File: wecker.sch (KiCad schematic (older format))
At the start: 2 parts, among them J1 Conn_01x20, U1 MSP430FR4133

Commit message: added some more parts
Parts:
- added C1, C2, C3, C4: 0.1µF, Capacitor_SMD:C_1206_3216Metric_Pad1.42x1.75mm_HandSolder, symbol Device:C
- added D1, D2: LED_BG, LED_SMD:LED_1210_3225Metric_Pad1.42x2.65mm_HandSolder, symbol Device:LED
- added J2: Conn_01x05_Male, Connector_PinHeader_2.54mm:PinHeader_1x05_P2.54mm_Horizontal, symbol Connector:Conn_01x05_Male
- added Q1: PN2222A, Package_TO_SOT_THT:TO-92_Inline, symbol Transistor_BJT:PN2222A
- added R1: R, Resistor_SMD:R_1210_3225Metric_Pad1.42x2.65mm_HandSolder, symbol Device:R
- added SW1: Hour, Button_Switch_SMD:SW_SPST_B3U-1000P, symbol Switch:SW_Push
- added SW2: Minute, Button_Switch_SMD:SW_SPST_B3U-1000P, symbol Switch:SW_Push
- added SW3: Snooze, Button_Switch_SMD:SW_SPST_B3U-1000P, symbol Switch:SW_Push
- added TP1: ClockInput, Connector_Wire:SolderWirePad_1x01_Drill1.2mm, symbol Connector:TestPoint
- added Y1: 32.768 kHz, Crystal:Crystal_HC18-U_Horizontal, symbol Device:Crystal_Small
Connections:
- net labels added: +BATT, GND
- wire segments 80 -> 162

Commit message: exchange some parts
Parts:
- removed Q1: PN2222A, Package_TO_SOT_THT:TO-92_Inline, symbol Transistor_BJT:PN2222A
- added Q1: BC818, Package_TO_SOT_SMD:SOT-23, symbol Transistor_BJT:BC818
- J2: footprint Connector_PinHeader_2.54mm:PinHeader_1x05_P2.54mm_Horizontal -> Connector_PinHeader_2.54mm:PinHeader_1x05_P2.54mm_Vertical
- Y1: footprint Crystal:Crystal_HC18-U_Horizontal -> Crystal:Crystal_DS26_D2.0mm_L6.0mm_Horizontal
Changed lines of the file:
@@
 F 0 "Y1" H 2600 4850 50  0000 C CNN
 F 1 "32.768 kHz" H 2600 5050 50  0000 C CNN
-F 2 "Crystal:Crystal_HC18-U_Horizontal" H 2600 4950 50  0001 C CNN
+F 2 "Crystal:Crystal_DS26_D2.0mm_L6.0mm_Horizontal" H 2600 4950 50  0001 C CNN
 F 3 "~" H 2600 4950 50  0001 C CNN
 	1    2600 4950
@@
 F 0 "J2" V 5112 3194 50  0000 L CNN
 F 1 "Conn_01x05_Male" V 5203 3194 50  0000 L CNN
-F 2 "Connector_PinHeader_2.54mm:PinHeader_1x05_P2.54mm_Horizontal" H 5050 2950 50  0001 C CNN
+F 2 "Connector_PinHeader_2.54mm:PinHeader_1x05_P2.54mm_Vertical" H 5050 2950 50  0001 C CNN
 F 3 "~" H 5050 2950 50  0001 C CNN
 	1    5050 2950
@@
 	9050 4550 9450 4550
 $Comp
-L Transistor_BJT:PN2222A Q1
-U 1 1 5DB2D7A4
-P 9650 4550
-F 0 "Q1" H 9840 4596 50  0000 L CNN
-F 1 "PN2222A" H 9840 4505 50  0000 L CNN
-F 2 "Package_TO_SOT_THT:TO-92_Inline" H 9850 4475 50  0001 L CIN
-F 3 "http://www.fairchildsemi.com/ds/PN/PN2222A.pdf" H 9650 4550 50  0001 L CNN
-	1    9650 4550
-	1    0    0    -1
-$EndComp
-$Comp
 L power:+BATT #PWR0108
 U 1 1 5DB2F2CF
@@
 Wire Wire Line
 	9750 4850 9750 4750
+$Comp
+L Transistor_BJT:BC818 Q1
+U 1 1 5DA08DFD
+P 9650 4550
+F 0 "Q1" H 9841 4596 50  0000 L CNN
+F 1 "BC818" H 9841 4505 50  0000 L CNN
+F 2 "Package_TO_SOT_SMD:SOT-23" H 9850 4475 50  0001 L CIN
+F 3 "https://www.fairchildsemi.com/datasheets/BC/BC818.pdf" H 9650 4550 50  0001 L CNN
+	1    9650 4550
+	1    0    0    -1
+$EndComp
 $EndSCHEMATC

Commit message: correct PCB Measurements
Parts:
- J2: symbol Connector:Conn_01x05_Male -> wecker-rescue:Conn_01x05_Male-Connector
- TP1: symbol Connector:TestPoint -> wecker-rescue:TestPoint-Connector
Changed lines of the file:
@@
 $EndComp
 $Comp
-L Connector:TestPoint TP1
+L wecker-rescue:TestPoint-Connector TP1
 U 1 1 5DAABA72
 P 7250 4550
@@
 	7900 5050 5350 5050
 $Comp
-L Connector:Conn_01x05_Male J2
+L wecker-rescue:Conn_01x05_Male-Connector J2
 U 1 1 5DAD772A
 P 5050 2950

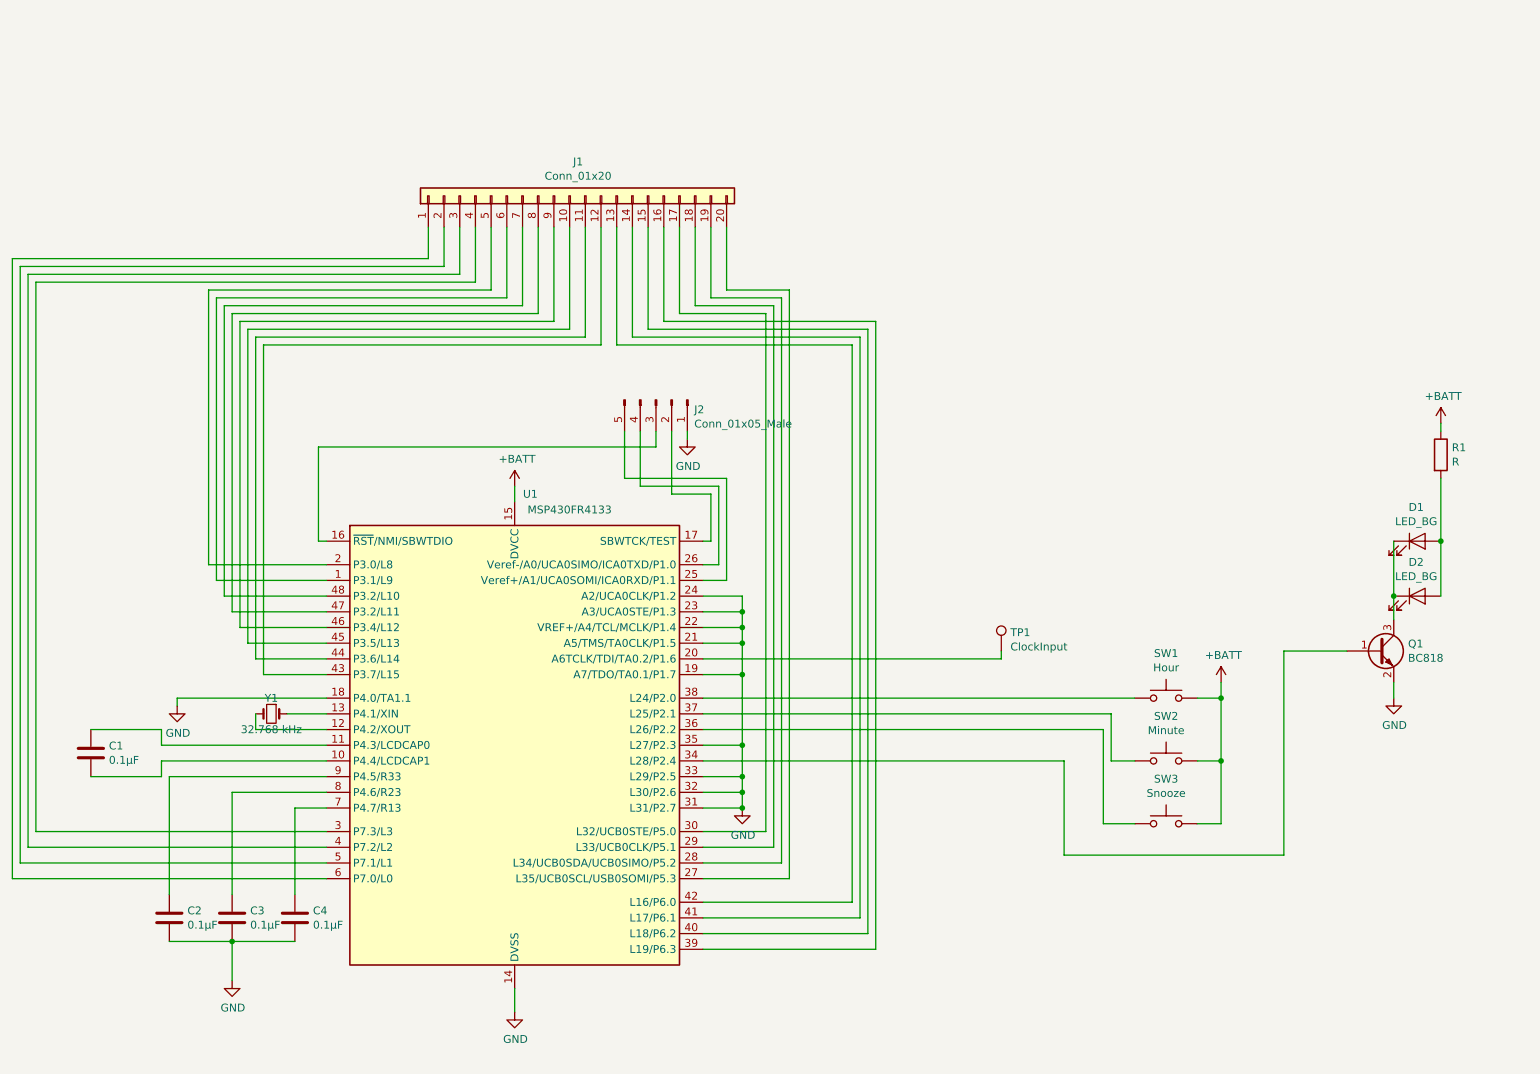
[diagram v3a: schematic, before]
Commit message: added Buzzer make LCD Bus
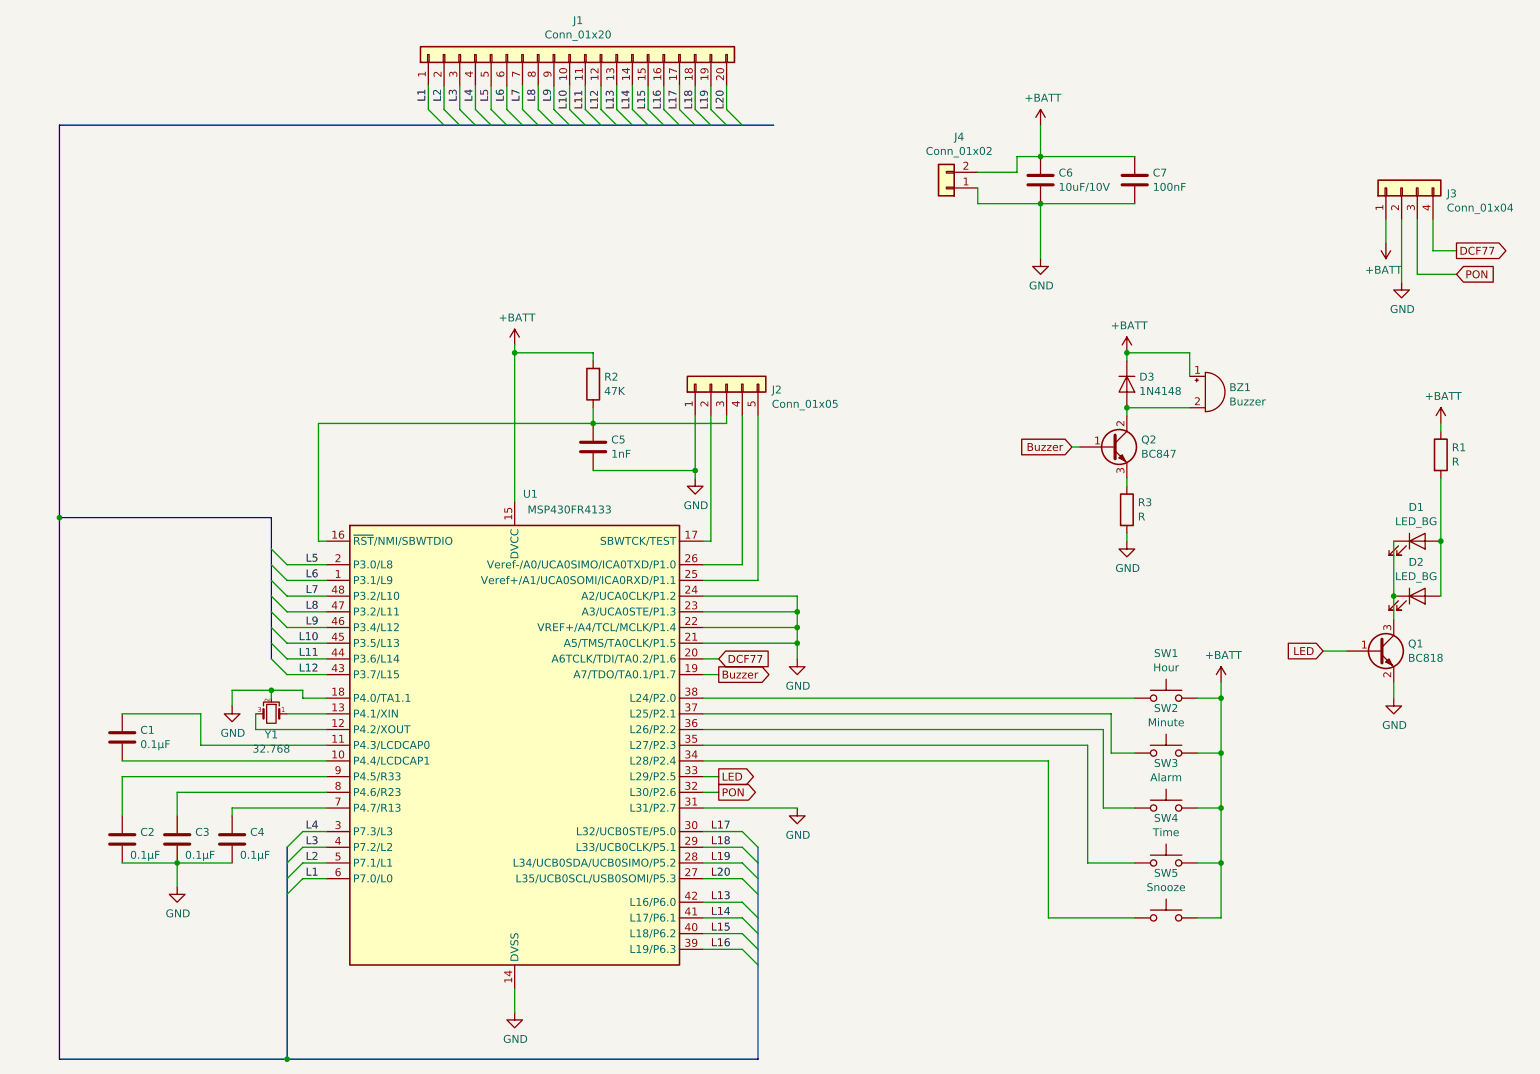
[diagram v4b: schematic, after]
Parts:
- removed J2: Conn_01x05_Male, Connector_PinHeader_2.54mm:PinHeader_1x05_P2.54mm_Vertical, symbol wecker-rescue:Conn_01x05_Male-Connector
- removed TP1: ClockInput, Connector_Wire:SolderWirePad_1x01_Drill1.2mm, symbol wecker-rescue:TestPoint-Connector
- removed Y1: 32.768 kHz, Crystal:Crystal_DS26_D2.0mm_L6.0mm_Horizontal, symbol Device:Crystal_Small
- added BZ1: Buzzer, symbol Device:Buzzer
- added C5: 1nF, symbol Device:C
- added C6: 10uF/10V, symbol Device:C
- added C7: 100nF, symbol Device:C
- added D3: 1N4148, symbol Device:D
- added J2: Conn_01x05, symbol Connector_Generic:Conn_01x05
- added J3: Conn_01x04, symbol Connector_Generic:Conn_01x04
- added J4: Conn_01x02, symbol Connector_Generic:Conn_01x02
- added Q2: BC847, symbol Device:Q_NPN_BCE
- added R2: 47K, symbol Device:R
- added R3: R, symbol Device:R
- added SW4: Time, Button_Switch_SMD:SW_SPST_B3U-1000P, symbol Switch:SW_Push
- added SW5: Snooze, Button_Switch_SMD:SW_SPST_B3U-1000P, symbol Switch:SW_Push
- added Y1: 32.768, symbol Device:Crystal_GND2_Small
- SW3: value Snooze -> Alarm
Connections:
- net +BATT: now also BZ1.1 (-), C6.1, C7.1, D3.1 (K), J3.1 (Pin_1), J4.2 (Pin_2), R2.2, SW4.2, SW5.2
- net GND: now also C5.1, C6.2, C7.2, J2.1 (Pin_1), J3.2 (Pin_2), J4.1 (Pin_1), R3.2, Y1.2; no longer U1.19 (A7/TDO/TA0.1/P1.7), U1.32 (L30/P2.6), U1.33 (L29/P2.5), U1.35 (L27/P2.3)
- net L6: now reaches J1.6 (Pin_6), U1.1 (P3.1/L9)
- net at U1.12 (P4.2/XOUT): now also Y1.3
- net at U1.13 (P4.1/XIN): now also Y1.1
- net at U1.16 (~RST~/NMI/SBWTDIO): now also C5.2, J2.3 (Pin_3), R2.1
- net at U1.17 (SBWTCK/TEST): now also J2.2 (Pin_2)
- net L5: now reaches J1.5 (Pin_5), U1.2 (P3.0/L8)
- net DCF77: now reaches U1.20 (A6TCLK/TDI/TA0.2/P1.6)
- net DCF77: now also J3.4 (Pin_4)
- net at U1.25 (Veref+/A1/UCA0SOMI/ICA0RXD/P1.1): now also J2.5 (Pin_5)
- net at U1.26 (Veref-/A0/UCA0SIMO/ICA0TXD/P1.0): now also J2.4 (Pin_4)
- net L20: now reaches J1.20 (Pin_20), U1.27 (L35/UCB0SCL/USB0SOMI/P5.3)
- net L19: now reaches J1.19 (Pin_19), U1.28 (L34/UCB0SDA/UCB0SIMO/P5.2)
- net L18: now reaches J1.18 (Pin_18), U1.29 (L33/UCB0CLK/P5.1)
- net L4: now reaches J1.4 (Pin_4), U1.3 (P7.3/L3)
- net L17: now reaches J1.17 (Pin_17), U1.30 (L32/UCB0STE/P5.0)
- net at U1.34 (L28/P2.4): now also SW5.1; no longer Q1.1 (B)
- net L16: now reaches J1.16 (Pin_16), U1.39 (L19/P6.3)
- net L3: now reaches J1.3 (Pin_3), U1.4 (P7.2/L2)
- net L15: now reaches J1.15 (Pin_15), U1.40 (L18/P6.2)
- net L14: now reaches J1.14 (Pin_14), U1.41 (L17/P6.1)
- net L13: now reaches J1.13 (Pin_13), U1.42 (L16/P6.0)
- net L12: now reaches J1.12 (Pin_12), U1.43 (P3.7/L15)
- net L11: now reaches J1.11 (Pin_11), U1.44 (P3.6/L14)
- net L10: now reaches J1.10 (Pin_10), U1.45 (P3.5/L13)
- net L9: now reaches J1.9 (Pin_9), U1.46 (P3.4/L12)
- net L8: now reaches J1.8 (Pin_8), U1.47 (P3.2/L11)
- net L7: now reaches J1.7 (Pin_7), U1.48 (P3.2/L10)
- net L2: now reaches J1.2 (Pin_2), U1.5 (P7.1/L1)
- net L1: now reaches J1.1 (Pin_1), U1.6 (P7.0/L0)
- new net: SW4.1, U1.35 (L27/P2.3)
- new net: BZ1.2 (+), D3.2 (A), Q2.2 (C)
- new net: Q2.3 (E), R3.1
- new net Buzzer: Q2.1 (B), U1.19 (A7/TDO/TA0.1/P1.7)
- new net LED: Q1.1 (B), U1.33 (L29/P2.5)
- new net PON: J3.3 (Pin_3), U1.32 (L30/P2.6)
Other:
- moved on the sheet: C1, C2, C3, C4, J1, SW2, SW3

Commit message: still not ready
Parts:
- added C8, C9: 12p, Capacitor_SMD:C_0603_1608Metric_Pad1.05x0.95mm_HandSolder, symbol Device:C_Small
- BZ1: footprint (none) -> Buzzer_Beeper:Buzzer_12x9.5RM7.6
- C1: value 0.1µF -> 1u; symbol Device:C -> Device:C_Small
- C2, C3, C4: value 0.1µF -> 100n; symbol Device:C -> Device:C_Small
- C5: footprint (none) -> Capacitor_SMD:C_1206_3216Metric_Pad1.42x1.75mm_HandSolder
- C6: value 10uF/10V -> 10u/10V; footprint (none) -> Capacitor_SMD:C_0603_1608Metric_Pad1.05x0.95mm_HandSolder
- C7: value 100nF -> 100n; footprint (none) -> Capacitor_SMD:C_1206_3216Metric_Pad1.42x1.75mm_HandSolder
- D3: footprint (none) -> Diode_SMD:D_0805_2012Metric_Pad1.15x1.40mm_HandSolder
- J2: footprint (none) -> Connector_PinHeader_2.54mm:PinHeader_1x05_P2.54mm_Horizontal
- J3: footprint (none) -> Connector_PinHeader_2.54mm:PinHeader_1x04_P2.54mm_Horizontal
- J4: footprint (none) -> Connector_PinHeader_2.54mm:PinHeader_1x02_P2.54mm_Horizontal
- Q2: value BC847 -> BC847; footprint (none) -> Package_TO_SOT_SMD:SOT-23
- R1: footprint Resistor_SMD:R_1210_3225Metric_Pad1.42x2.65mm_HandSolder -> Resistor_SMD:R_0603_1608Metric_Pad1.05x0.95mm_HandSolder
- R2, R3: footprint (none) -> Resistor_SMD:R_0603_1608Metric_Pad1.05x0.95mm_HandSolder
- Y1: footprint (none) -> Crystal:Crystal_DS26_D2.0mm_L6.0mm_Horizontal_1EP_style1
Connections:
- net GND: now also C8.2, C9.2; no longer U1.18 (P4.0/TA1.1), U1.21 (A5/TMS/TA0CLK/P1.5), U1.22 (VREF+/A4/TCL/MCLK/P1.4), U1.23 (A3/UCA0STE/P1.3), U1.24 (A2/UCA0CLK/P1.2), U1.31 (L31/P2.7)
- net at U1.12 (P4.2/XOUT), Y1.3: now also C9.1
- net at U1.13 (P4.1/XIN), Y1.1: now also C8.1
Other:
- note added: "DNP"
- moved on the sheet: C1, C2, C3, C4, Y1

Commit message: some more corrections
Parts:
- removed D3: 1N4148, Diode_SMD:D_0805_2012Metric_Pad1.15x1.40mm_HandSolder, symbol Device:D
- added R4: 1k, Resistor_SMD:R_0805_2012Metric_Pad1.15x1.40mm_HandSolder, symbol Device:R
- BZ1: footprint Buzzer_Beeper:Buzzer_12x9.5RM7.6 -> Buzzer_Beeper:Buzzer_TDK_PS1240P02BT_D12.2mm_H6.5mm
- C1, C2, C3, C4, C5, C7: footprint Capacitor_SMD:C_1206_3216Metric_Pad1.42x1.75mm_HandSolder -> Capacitor_SMD:C_0805_2012Metric_Pad1.15x1.40mm_HandSolder
- C6, C8, C9: footprint Capacitor_SMD:C_0603_1608Metric_Pad1.05x0.95mm_HandSolder -> Capacitor_SMD:C_0805_2012Metric_Pad1.15x1.40mm_HandSolder
- R1, R3: value R -> 1K; footprint Resistor_SMD:R_0603_1608Metric_Pad1.05x0.95mm_HandSolder -> Resistor_SMD:R_0805_2012Metric_Pad1.15x1.40mm_HandSolder
- R2: footprint Resistor_SMD:R_0603_1608Metric_Pad1.05x0.95mm_HandSolder -> Resistor_SMD:R_0805_2012Metric_Pad1.15x1.40mm_HandSolder
- Y1: symbol Device:Crystal_GND2_Small -> Device:Crystal_GND3_Small
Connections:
- net +BATT: now also D1.2 (A), D2.2 (A), R4.1; no longer R1.1
- net Buzzer: now also R3.1; no longer Q2.1 (B)
- net GND: now also Q2.3 (E); no longer C8.2, C9.2, R3.2, Y1.2
- net LED: now also R1.1; no longer Q1.1 (B)
- net at C8.1, Y1.1: now also U1.12 (P4.2/XOUT); no longer U1.13 (P4.1/XIN)
- net at BZ1.2 (+), Q2.2 (C): now also R4.2
- new net: C9.1, U1.13 (P4.1/XIN), Y1.2
- new net: Q1.1 (B), R1.2
- new net: Q2.1 (B), R3.2
- new net GNDS: C8.2, C9.2, Y1.3
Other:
- moved on the sheet: D1, D2, Q1, R1, R3

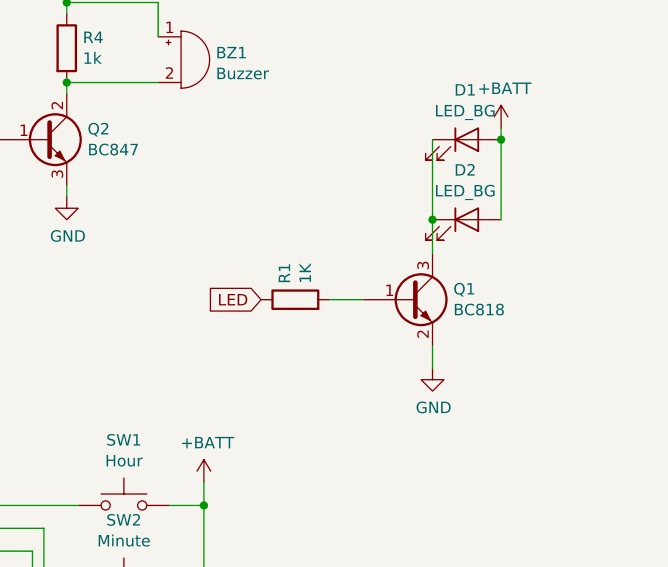
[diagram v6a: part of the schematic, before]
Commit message: set LED Rb and Tr Type
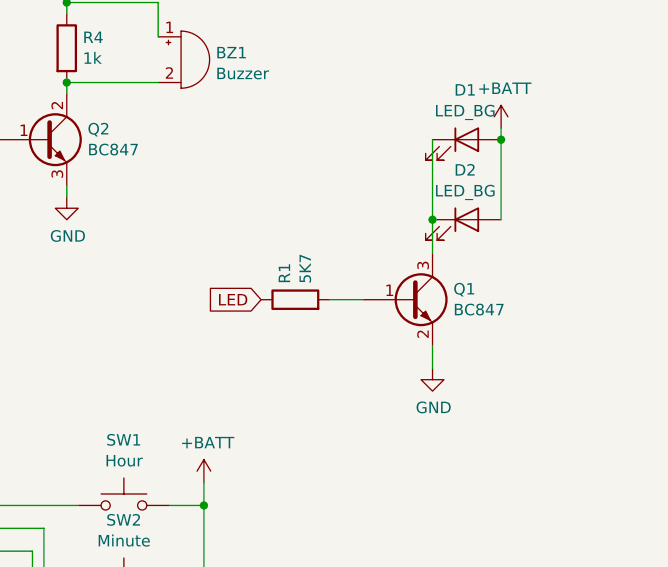
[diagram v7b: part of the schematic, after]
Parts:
- Q1: value BC818 -> BC847
- R1: value 1K -> 5K7
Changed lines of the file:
@@
 P 9050 3950
 F 0 "R1" H 9120 3996 50  0000 L CNN
-F 1 "1K" H 9120 3905 50  0000 L CNN
+F 1 "5K7" H 9120 3905 50  0000 L CNN
 F 2 "Resistor_SMD:R_0805_2012Metric_Pad1.15x1.40mm_HandSolder" V 8980 3950 50  0001 C CNN
 F 3 "~" H 9050 3950 50  0001 C CNN
@@
 P 9550 3950
 F 0 "Q1" H 9741 3996 50  0000 L CNN
-F 1 "BC818" H 9741 3905 50  0000 L CNN
+F 1 "BC847" H 9741 3905 50  0000 L CNN
 F 2 "Package_TO_SOT_SMD:SOT-23" H 9750 3875 50  0001 L CIN
 F 3 "https://www.fairchildsemi.com/datasheets/BC/BC818.pdf" H 9550 3950 50  0001 L CNN
